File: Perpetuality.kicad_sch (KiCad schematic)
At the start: 27 parts, among them J1 Conn_01x04, J2 Conn_01x01, J3 Conn_01x01, J4 Conn_01x01, U1 XIAO-nRF52840-SMD, U2 NCV8164CSN180T1G, U3 ICM-20948, U4 INA333xxDGK, U5 OPA333xxDCK, U6 ADS8866IDGS

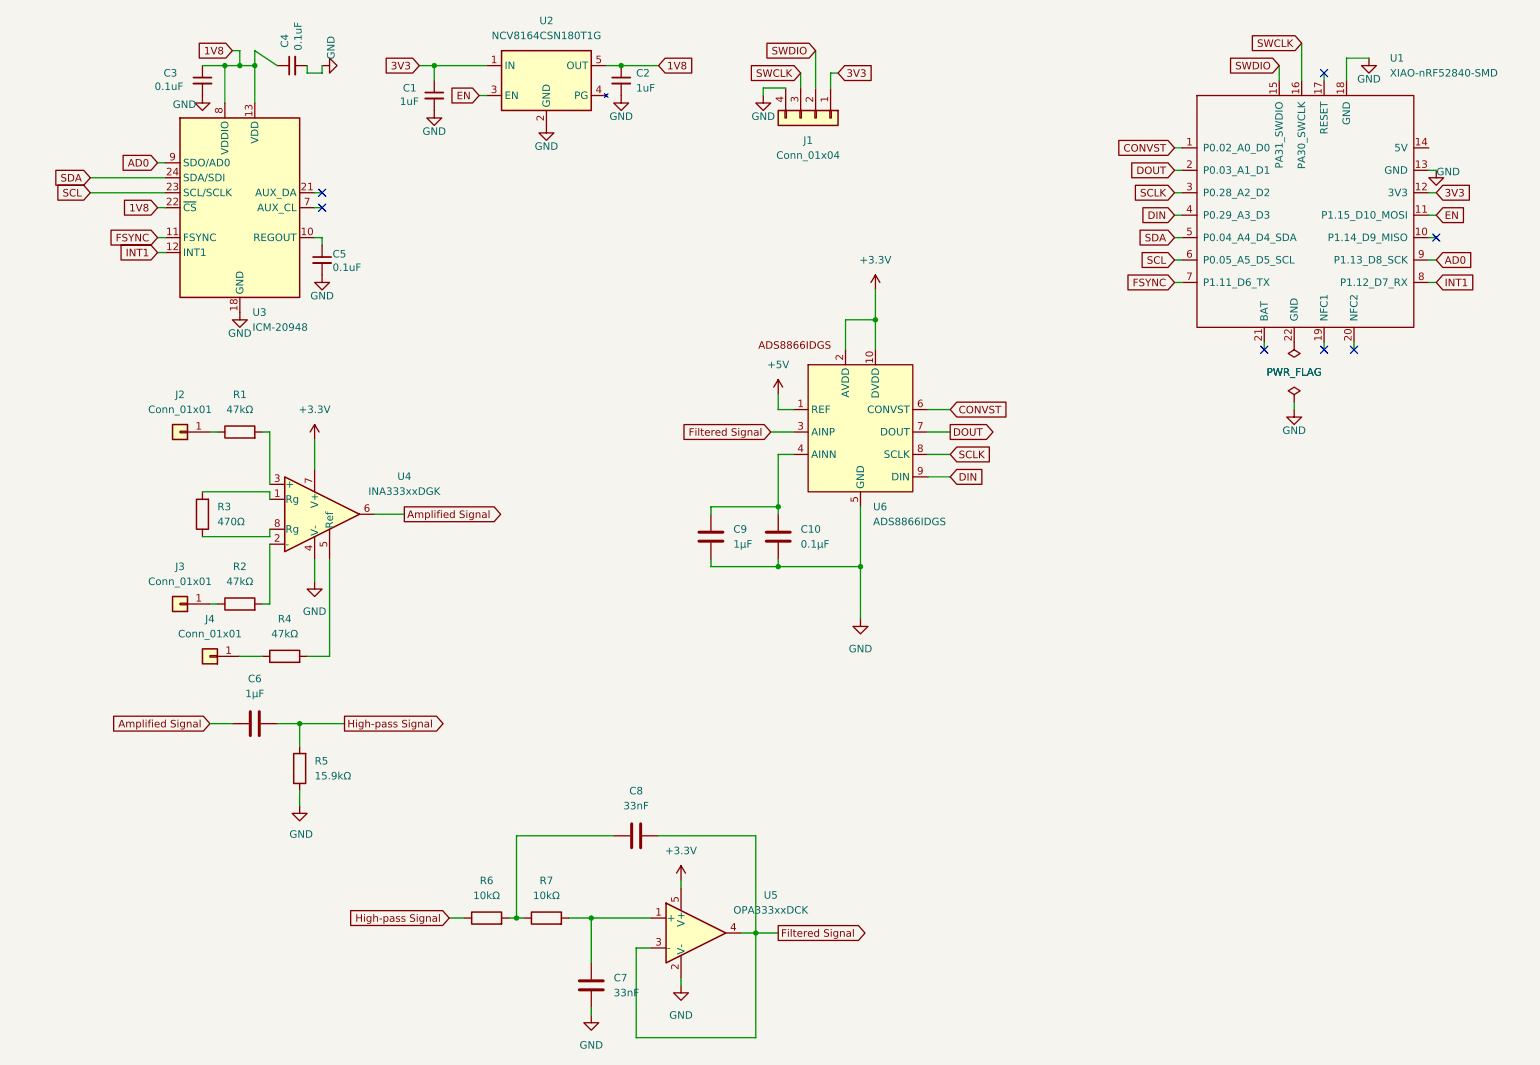
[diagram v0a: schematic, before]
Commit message: OG Schematic Redesign
Implemented a cheaper, more-suitable ADS7924IRTER (with a dedicated MCP1501T-33E/SN "series" voltage reference) to allow for 4x EMG sensor circuits. Added appropriate decoupling capacitors and fixed pin configurations to improve the original prototype schematic.
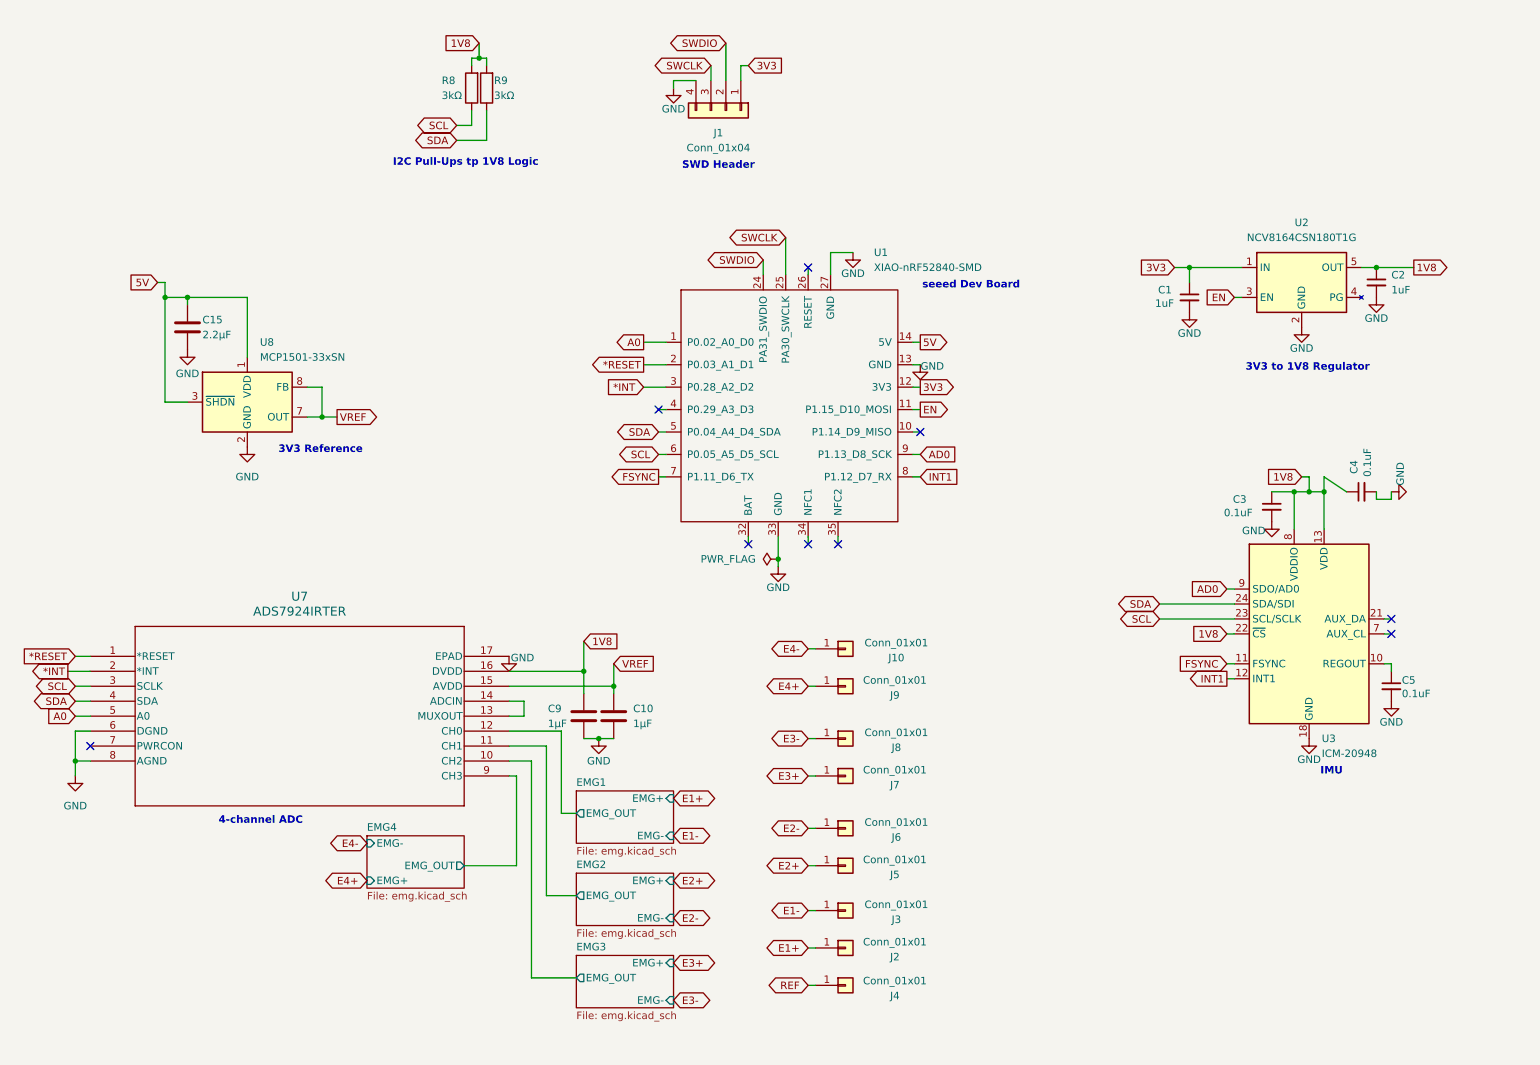
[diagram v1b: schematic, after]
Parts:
- removed C6: 1µF, Capacitor_SMD:C_0603_1608Metric, symbol Device:C
- removed C7, C8: 33nF, Capacitor_SMD:C_0603_1608Metric, symbol Device:C
- removed R1, R2, R4: 47kΩ, Resistor_SMD:R_0603_1608Metric, symbol Device:R
- removed R3: 470Ω, Resistor_SMD:R_0603_1608Metric, symbol Device:R
- removed R5: 15.9kΩ, Resistor_SMD:R_0603_1608Metric, symbol Device:R
- removed R6, R7: 10kΩ, Resistor_SMD:R_0603_1608Metric, symbol Device:R
- removed U4: INA333xxDGK, Package_SO:VSSOP-8_3x3mm_P0.65mm, symbol Amplifier_Instrumentation:INA333xxDGK
- removed U5: OPA333xxDCK, Package_TO_SOT_SMD:SOT-353_SC-70-5, symbol Amplifier_Operational:OPA333xxDCK
- removed U6: ADS8866IDGS, perpetuality_footprints:DGS0010A_L, symbol ADC:ADS8866IDGS
- added C15: 2.2µF, Capacitor_SMD:C_0603_1608Metric, symbol Device:C
- added J10, J5, J6, J7, J8, J9: Conn_01x01, Connector_PinHeader_2.00mm:PinHeader_1x01_P2.00mm_Vertical, symbol Connector_Generic:Conn_01x01
- added R8, R9: 3kΩ, symbol Device:R
- added U7: ADS7924IRTER, perpetuality_footprints:RTE16_1P7X1P7, symbol lib:ADS7924IRTER
- added U8: MCP1501-33xSN, Package_SO:SOIC-8_3.9x4.9mm_P1.27mm, symbol Reference_Voltage:MCP1501-33xSN
- C10: value 0.1µF -> 1µF
- U2: footprint Package_SO:TSOP-5_1.65x3.05mm_P0.95mm -> Package_TO_SOT_SMD:TSOT-23-5
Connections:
- net 1V8: now also C9.1, R8.2, R9.2, U7.16 (DVDD)
- net GND: now also U1.27 (GND), U1.33 (GND), C15.2, U7.17 (EPAD), U7.6 (DGND), U7.8 (AGND), U8.2 (GND), U8.4 (GND), U8.5 (GND), U8.6 (GND); no longer U1.18 (GND)
- net SCL: now also R8.1, U7.3 (SCLK)
- net SDA: now also R9.1, U7.4 (SDA)
- net SWCLK: now also U1.25 (PA30_SWCLK); no longer U1.16 (PA30_SWCLK)
- net SWDIO: now also U1.24 (PA31_SWDIO); no longer U1.15 (PA31_SWDIO)
- net VREF: now reaches C10.1
- net VREF: now also U7.15 (AVDD), U8.7 (OUT), U8.8 (FB); no longer C9.1
- net REF: now reaches J4.1 (Pin_1)
- net 5V: now reaches U1.14 (5V)
- net 5V: now also C15.1, U8.1 (VDD), U8.3 (~{SHDN})
- net E1+: now reaches J2.1 (Pin_1)
- net E1-: now reaches J3.1 (Pin_1)
- net CONVST renamed A0
- net A0: now also U7.5 (A0)
- net DIN: no longer names the net of U1.4 (P0.29_A3_D3)
- net DOUT renamed *RESET
- net *RESET: now also U7.1 (*RESET)
- net SCLK renamed *INT
- net *INT: now also U7.2 (*INT)
- new net: U7.13 (MUXOUT), U7.14 (ADCIN)
- new net E2+: J5.1 (Pin_1)
- new net E2-: J6.1 (Pin_1)
- new net E3+: J7.1 (Pin_1)
- new net E3-: J8.1 (Pin_1)
- new net E4+: J9.1 (Pin_1)
- new net E4-: J10.1 (Pin_1)
- new net EMG1/EMG_OUT: U7.12 (CH0)
- new net EMG2/EMG_OUT: U7.11 (CH1)
- new net EMG3/EMG_OUT: U7.10 (CH2)
- new net EMG4/EMG_OUT: U7.9 (CH3)
- no-connect marks 7 -> 9
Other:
- added sheet EMG1 (emg.kicad_sch)
- added sheet EMG2 (emg.kicad_sch)
- added sheet EMG3 (emg.kicad_sch)
- added sheet EMG4 (emg.kicad_sch)
- note added: "3V3 Reference"
- note added: "3V3 to 1V8 Regulator"
- note added: "4-channel ADC"
- note added: "I2C Pull-Ups tp 1V8 Logic"
- note added: "IMU"
- note added: "SWD Header"
- note added: "seeed Dev Board"
- moved on the sheet: C1, C10, C2, C3, C4, C5, C9, J1, J2, J3, J4, U1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

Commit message: newest version sent to jlc
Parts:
- added NT1: NetTie_2, symbol Device:NetTie_2
- J1: footprint Connector_PinHeader_2.00mm:PinHeader_1x04_P2.00mm_Vertical -> TestPoint:TestPoint_Pad_2.0x2.0mm
- J10, J2, J3, J4, J5, J6, J7, J8, J9: footprint Connector_PinHeader_2.00mm:PinHeader_1x01_P2.00mm_Vertical -> TestPoint:TestPoint_Pad_2.0x2.0mm
- R8, R9: footprint (none) -> Resistor_SMD:R_0603_1608Metric
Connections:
- net GND: now also NT1.2; no longer C1.2, C10.2, C15.2, C2.2, C3.2, C4.2, C5.2, C9.2, J1.4 (Pin_4), U1.13 (GND), U1.27 (GND), U1.33 (GND), U2.2 (GND), U3.18 (GND), U3.20 (GND), U7.6 (DGND), U8.2 (GND), U8.4 (GND), U8.5 (GND), U8.6 (GND)
- new net GNDD: C1.2, C10.2, C15.2, C2.2, C3.2, C4.2, C5.2, C9.2, J1.4 (Pin_4), NT1.1, U1.13 (GND), U1.27 (GND), U1.33 (GND), U2.2 (GND), U3.18 (GND), U3.20 (GND), U7.6 (DGND), U8.2 (GND), U8.4 (GND), U8.5 (GND), U8.6 (GND)
